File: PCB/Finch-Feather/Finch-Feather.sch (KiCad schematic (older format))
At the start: 30 parts

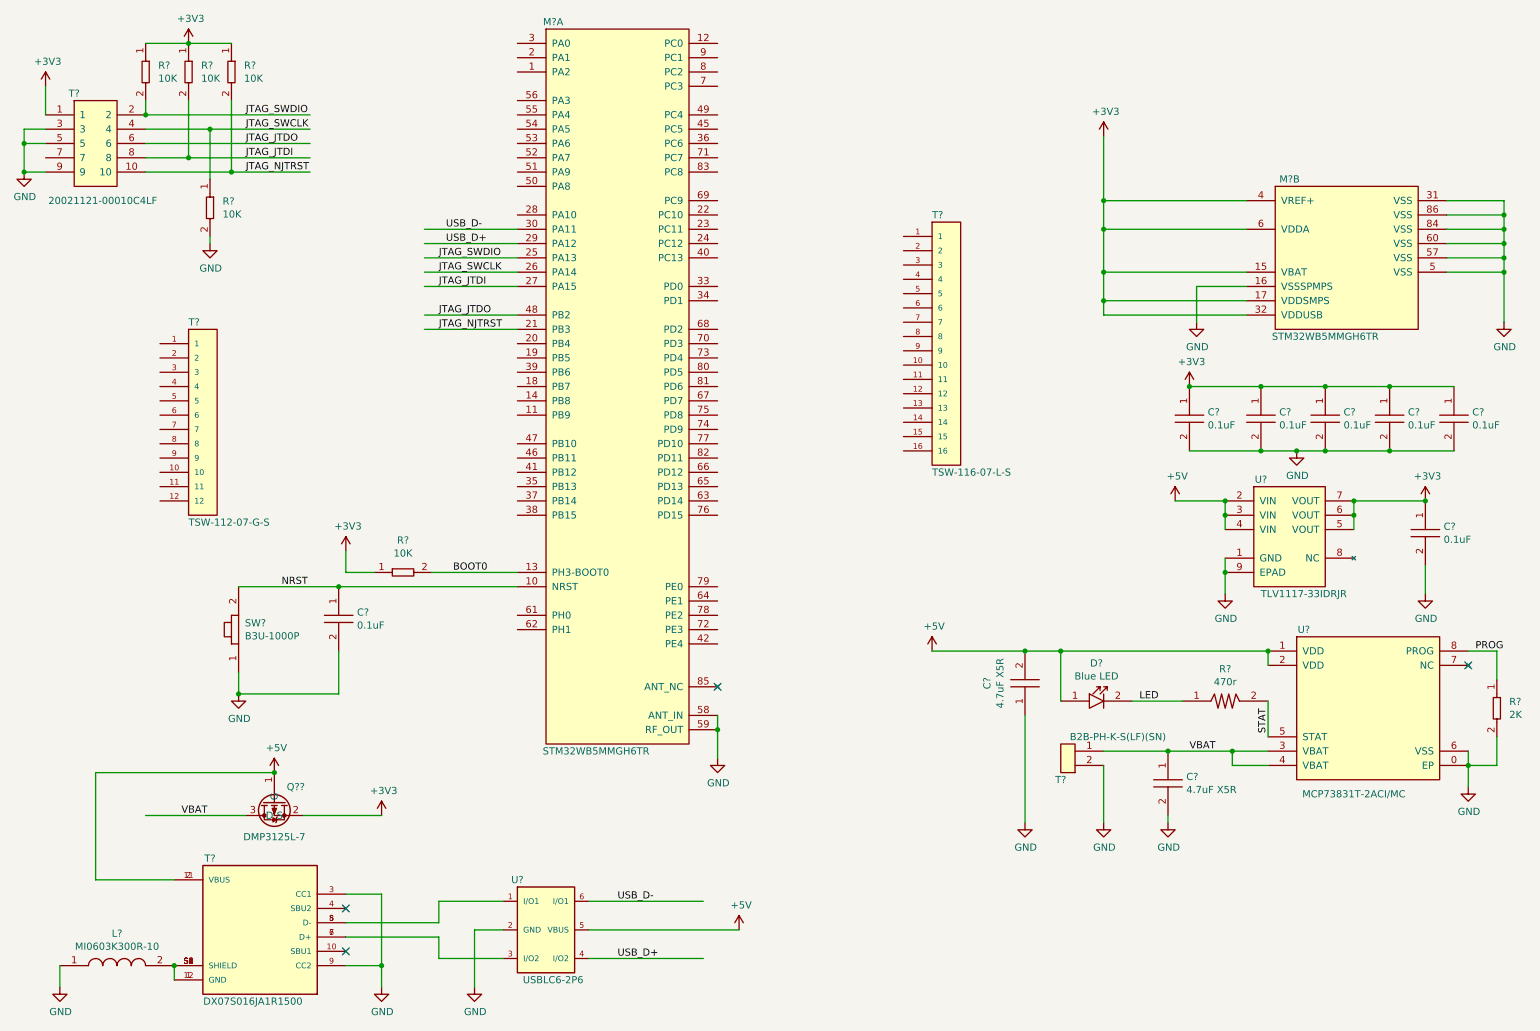
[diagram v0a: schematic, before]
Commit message: PCB
PCB started, next step figuring out which pins on module to use
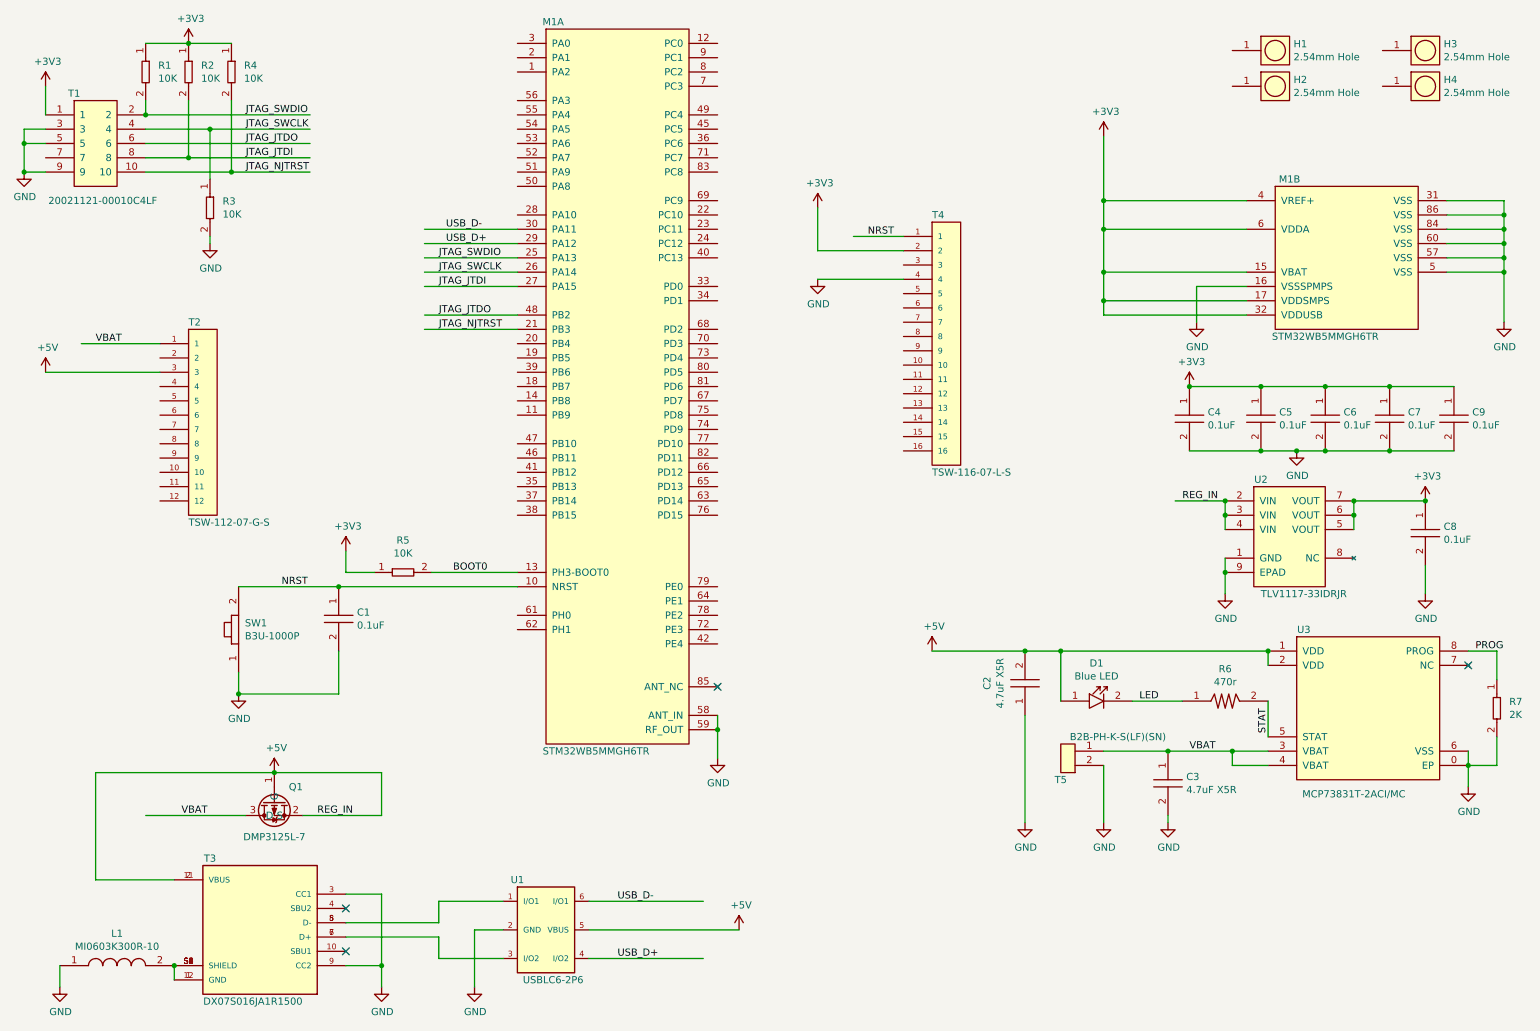
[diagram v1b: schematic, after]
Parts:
- added H1, H2, H3, H4: 2.54mm_PLT_Hole, AVR-KiCAD-Lib-Holes_Fasteners:2.54mm_PLT_Hole, symbol AVR-KiCAD-Lib-Holes_Fasteners:2.54mm_PLT_Hole
- gave numbers to parts that had none: 29
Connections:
- net labels added: REG_IN
- wire segments 123 -> 131

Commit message: PCB Near Finished
Head signals wired to pins on module, power supply section and USB connector are next
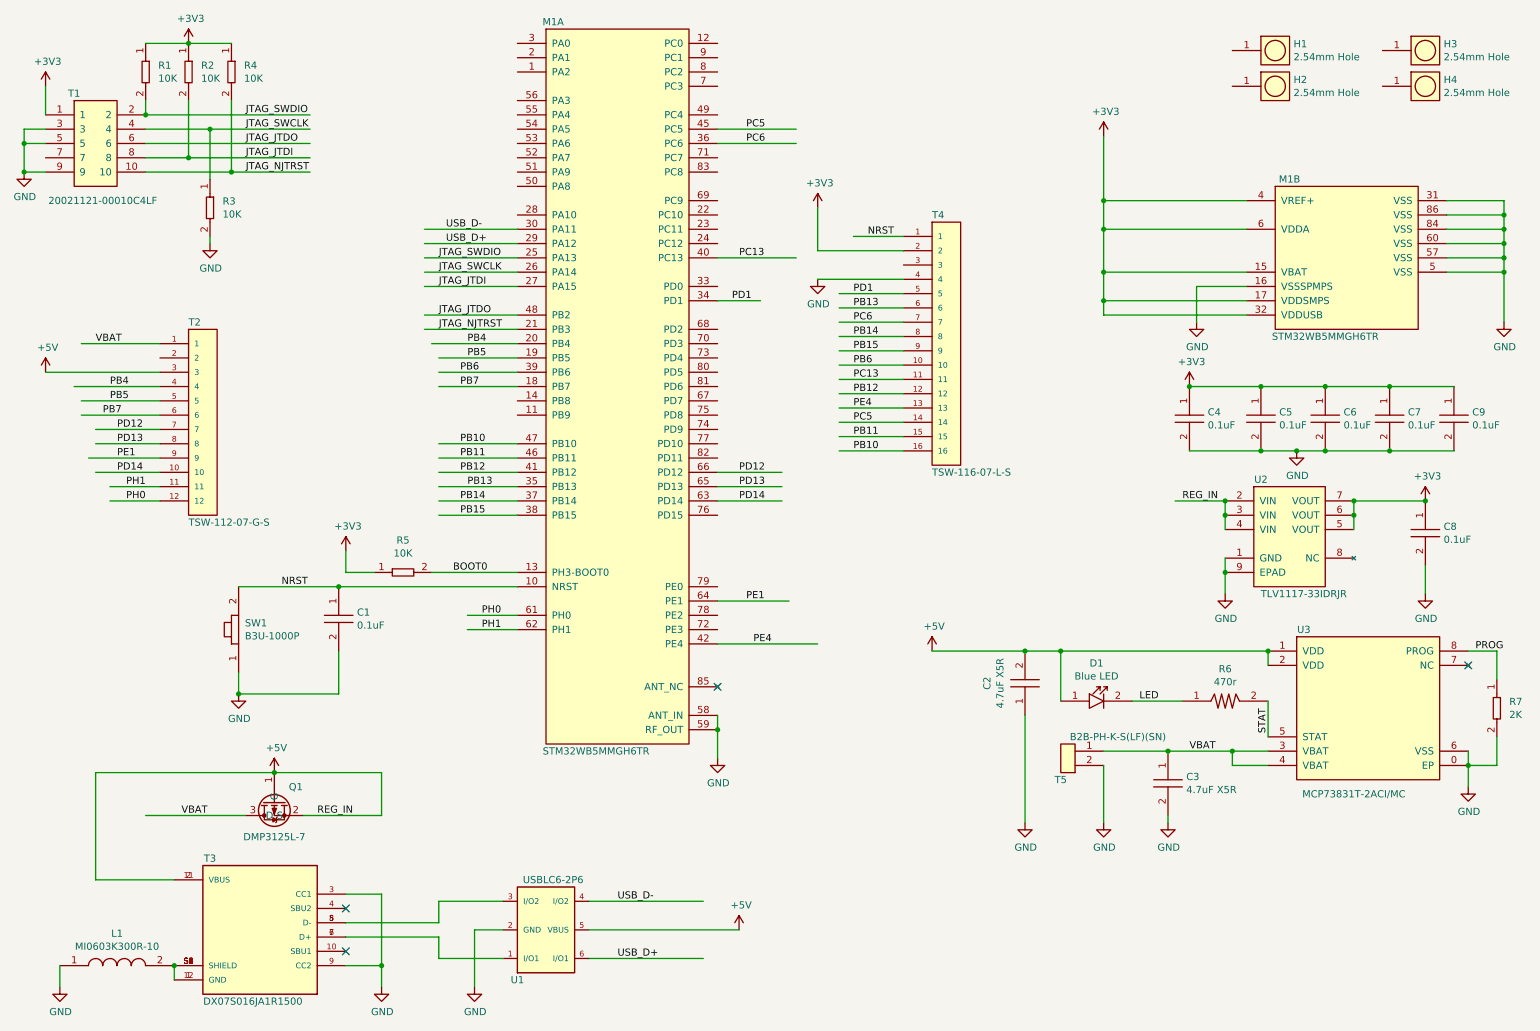
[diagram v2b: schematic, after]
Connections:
- net labels added: PB10, PB11, PB12, PB13, PB14, PB15, PB4, PB5, PB6, PB7, PC13, PC5, PC6, PD1, PD12, PD13, PD14, PE1, PE4, PH0, PH1
- wire segments 131 -> 173

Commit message: PCB Progress
More progress on PCB design, made some tweaks and changes, implemented enable circuit.
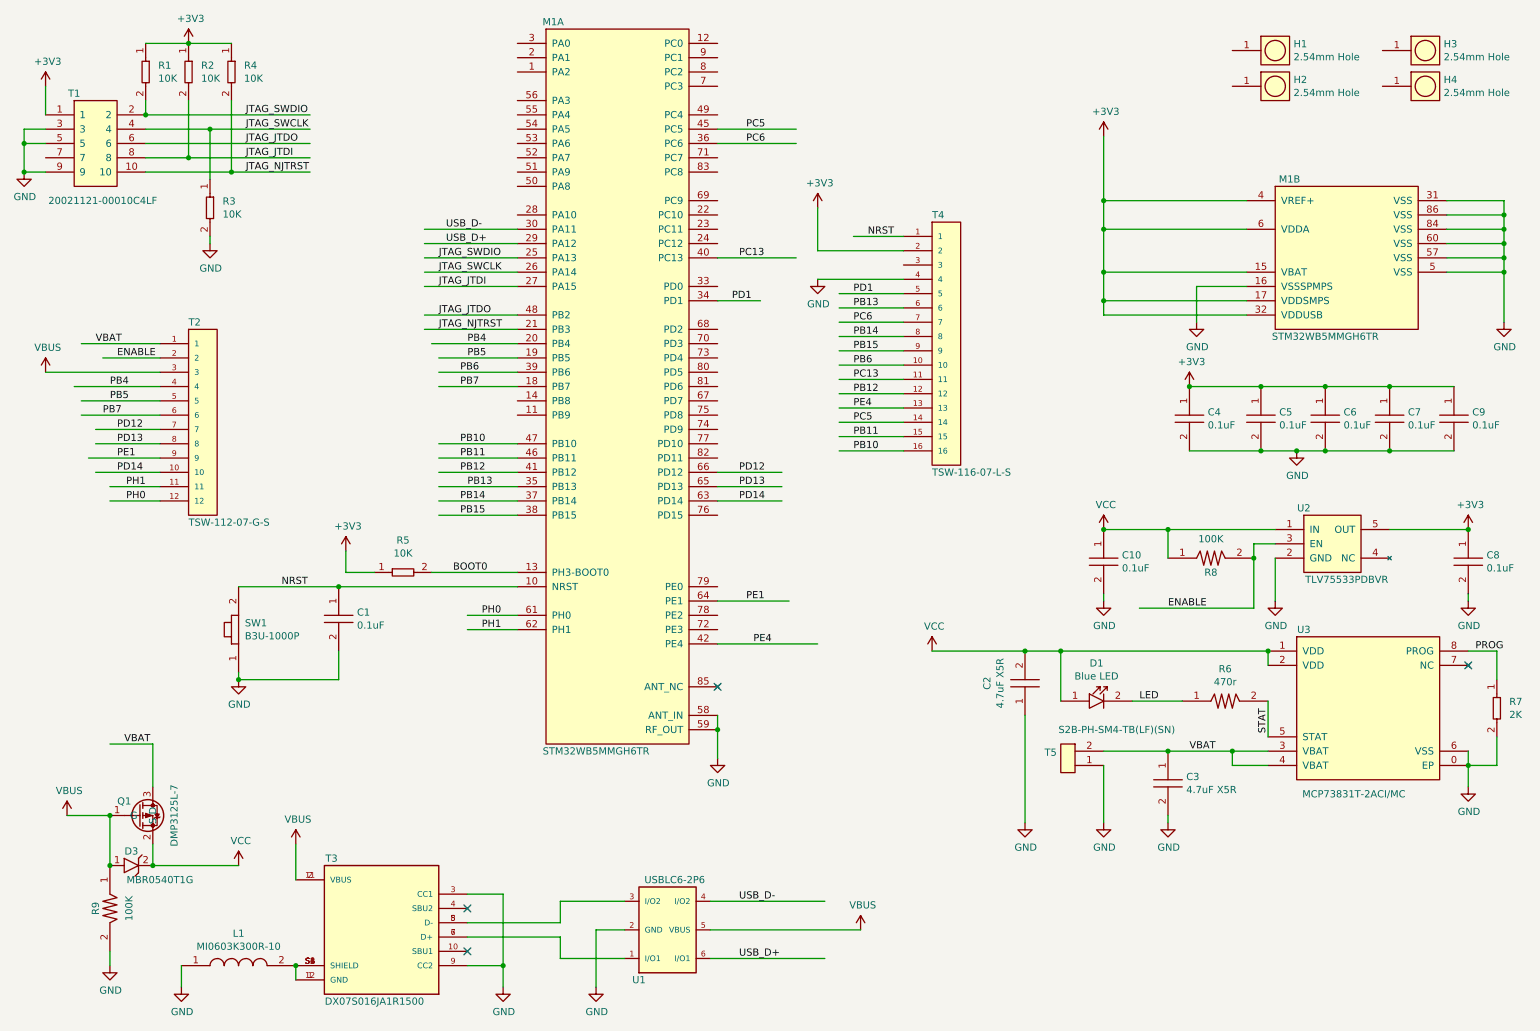
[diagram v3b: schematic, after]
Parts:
- removed T5: B2B-PH-K-S(LF)(SN), AVR-KiCAD-Lib-Connectors:B2B-PH-K-S(LF)(SN), symbol AVR-KiCAD-Lib-Connectors:B2B-PH-K-S(LF)(SN)
- removed U2: TLV1117-33IDRJR, AVR-KiCAD-Lib-ICs:TLV1117-33IDRJR, symbol AVR-KiCAD-Lib-ICs:TLV1117-33IDRJR
- added C10: C0402C104K9PACTU, AVR-KiCAD-Lib-Resistors:R0402, symbol AVR-KiCAD-Lib-Capacitors:C0402C104K9PACTU
- added D3: MBR0540T1G, AVR-KiCAD-Lib-Diodes:D_SOD-123, symbol AVR-KiCAD-Lib-Diodes:MBR0540T1G
- added R8, R9: RC0603FR-07100KL, AVR-KiCAD-Lib-Resistors:R0603, symbol AVR-KiCAD-Lib-Resistors:RC0603FR-07100KL
- added T5: S2B-PH-SM4-TB(LF)(SN), AVR-KiCAD-Lib-Connectors:B2B-PH-SM4-TB(LF)(SN), symbol AVR-KiCAD-Lib-Connectors:S2B-PH-SM4-TB(LF)(SN)
- added U2: TLV75533PDBVR, AVR-KiCAD-Lib-ICs:TLV75533PDBVR, symbol AVR-KiCAD-Lib-ICs:TLV75533PDBVR
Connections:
- net labels added: ENABLE, VBUS, VCC
- net labels removed: +5V, REG_IN
- wire segments 173 -> 177
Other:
- moved on the sheet: C8, L1, T3, U1

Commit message: PCB pass COmplete
First true pass of PCB fully complete, with new power switching circuit and regulator enable. Smaller packages selected for pretty much every IC previously used.
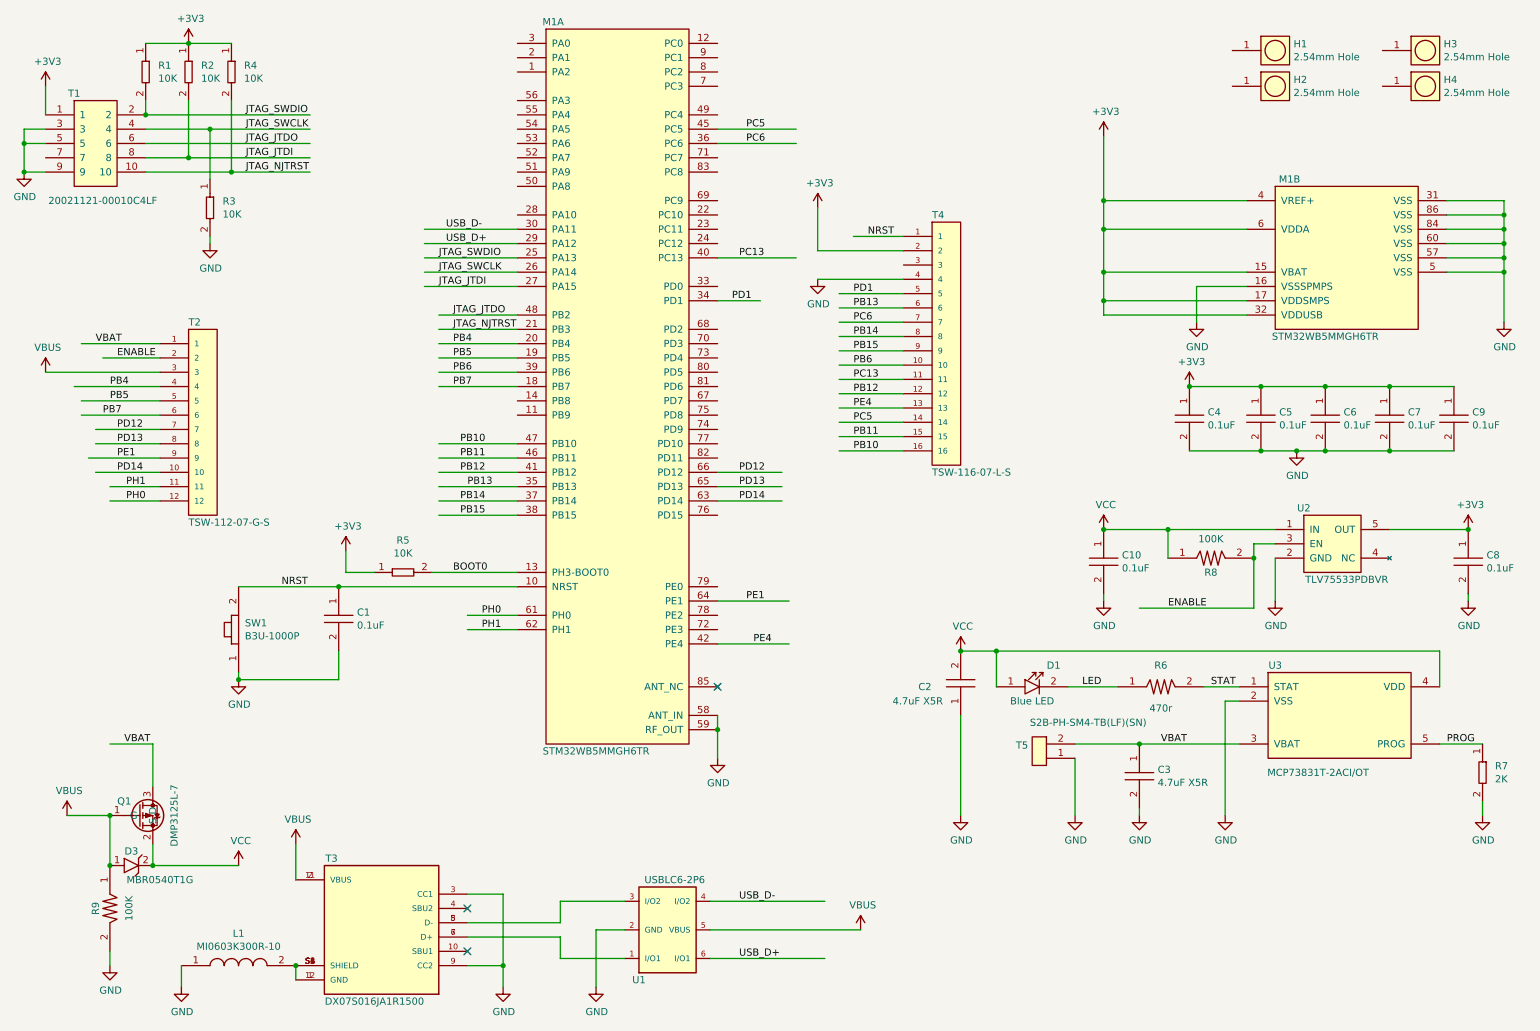
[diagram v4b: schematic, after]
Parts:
- removed U3: MCP73831T-2ACI_MC, AVR-KiCAD-Lib-ICs:MCP73831T-2ACI-MC, symbol AVR-KiCAD-Lib-ICs:MCP73831T-2ACI_MC
- added U3: MCP73831T-2ACI_OT, AVR-KiCAD-Lib-ICs:SOT-23-5, symbol AVR-KiCAD-Lib-ICs:MCP73831T-2ACI_OT
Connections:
- wire segments 177 -> 171
- no-connect marks 4 -> 3
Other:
- moved on the sheet: C2, C3, D1, R6, R7, T5
